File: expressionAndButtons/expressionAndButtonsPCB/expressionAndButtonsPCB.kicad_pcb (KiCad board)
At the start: 2 copper layers, 189.7 x 184.2 mm, 66 parts, among them J1 Alimentazione, J2 Input comandi, J3 OUTPUT C, J4 OUTPUT I, J5 OUTPUT III, J6 INPUT C-I-III, U2 ProMicro

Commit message: Progresso bottoniera
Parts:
- added J7: Conn_01x04, TerminalBlock_Phoenix:TerminalBlock_Phoenix_MPT-0,5-4-2.54_1x04_P2.54mm_Horizontal, F.Cu at (37.6, 105.4)
- added J8: Conn_01x04, TerminalBlock_Phoenix:TerminalBlock_Phoenix_MPT-0,5-4-2.54_1x04_P2.54mm_Horizontal, F.Cu at (214.4, 94.5)
- J2: value Input comandi -> Conn_01x12; footprint TerminalBlock_Phoenix:TerminalBlock_Phoenix_MKDS-1,5-16_1x16_P5.00mm_Horizontal -> TerminalBlock_Phoenix:TerminalBlock_Phoenix_MPT-0,5-12-2.54_1x12_P2.54mm_Horizontal
- J3: value OUTPUT C -> Conn_01x12; footprint TerminalBlock_Phoenix:TerminalBlock_Phoenix_MKDS-1,5-16_1x16_P5.00mm_Horizontal -> TerminalBlock_Phoenix:TerminalBlock_Phoenix_MPT-0,5-12-2.54_1x12_P2.54mm_Horizontal
- J4, J5: footprint TerminalBlock_Phoenix:TerminalBlock_Phoenix_MKDS-1,5-9-5.08_1x09_P5.08mm_Horizontal -> TerminalBlock_Phoenix:TerminalBlock_Phoenix_MPT-0,5-9-2.54_1x09_P2.54mm_Horizontal
- moved J3 19.9 mm to (214.4, 126.5)
- moved J2 14.7 mm to (37.6, 73.2)
- moved J4 8.93 mm to (90.4, 200.2)
- moved J5 8.52 mm to (147.3, 199.1)
- moved J6 6.73 mm to (38.4, 150.4)
- moved F1 5.22 mm to (56.6, 41.1)
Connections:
- Cresc2 pad 10: Net-(Cresc2-VCC) -> Net-(Cresc1-VCC)
- Cresc2 pad 13: Net-(Cresc2-VCC) -> Net-(Cresc1-VCC)
- Cresc2 pad 16: Net-(Cresc2-VCC) -> Net-(Cresc1-VCC)
- IN1 pad 7: Net-(IN1-~{Q7}) -> unconnected-(IN1-~{Q7}-Pad7)
- IN1 pad 9: unconnected-(IN1-Q7-Pad9) -> Net-(IN1-Q7)
- IN2 pad 10: Net-(IN1-~{Q7}) -> Net-(IN1-Q7)
- R29 pad 2: Net-(J3-Pin_13) -> Net-(J8-Pin_1)
- R30 pad 2: Net-(J3-Pin_14) -> Net-(J8-Pin_2)
- R31 pad 2: Net-(J3-Pin_15) -> Net-(J8-Pin_3)
- R32 pad 2: Net-(J3-Pin_16) -> Net-(J8-Pin_4)
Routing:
- net Net-(J6-Pin_3): track 0.00 -> 320.0 mm
- net Net-(J6-Pin_2): track 0.00 -> 312.7 mm
- net Net-(J6-Pin_1): track 0.00 -> 307.8 mm
- net Net-(Cresc1-VCC): track 101.4 -> 362.0 mm
- net Net-(IN2-D2): track 24.2 -> 179.5 mm
- net Net-(IN2-D3): track 24.1 -> 178.7 mm
- net Net-(IN2-D1): track 24.2 -> 176.2 mm
- net Net-(IN2-D7): track 24.1 -> 173.6 mm
- net Net-(IN2-D0): track 24.1 -> 172.7 mm
- net Net-(Cresc1-QA): track 0.00 -> 147.2 mm
- net Net-(IN2-D6): track 24.2 -> 164.2 mm
- net Net-(Cresc1-QB): track 0.00 -> 132.0 mm
- net Net-(IN2-D5): track 24.2 -> 155.6 mm
- net Net-(Cresc1-QC): track 0.00 -> 124.9 mm
- net Net-(IN2-D4): track 24.1 -> 145.6 mm
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
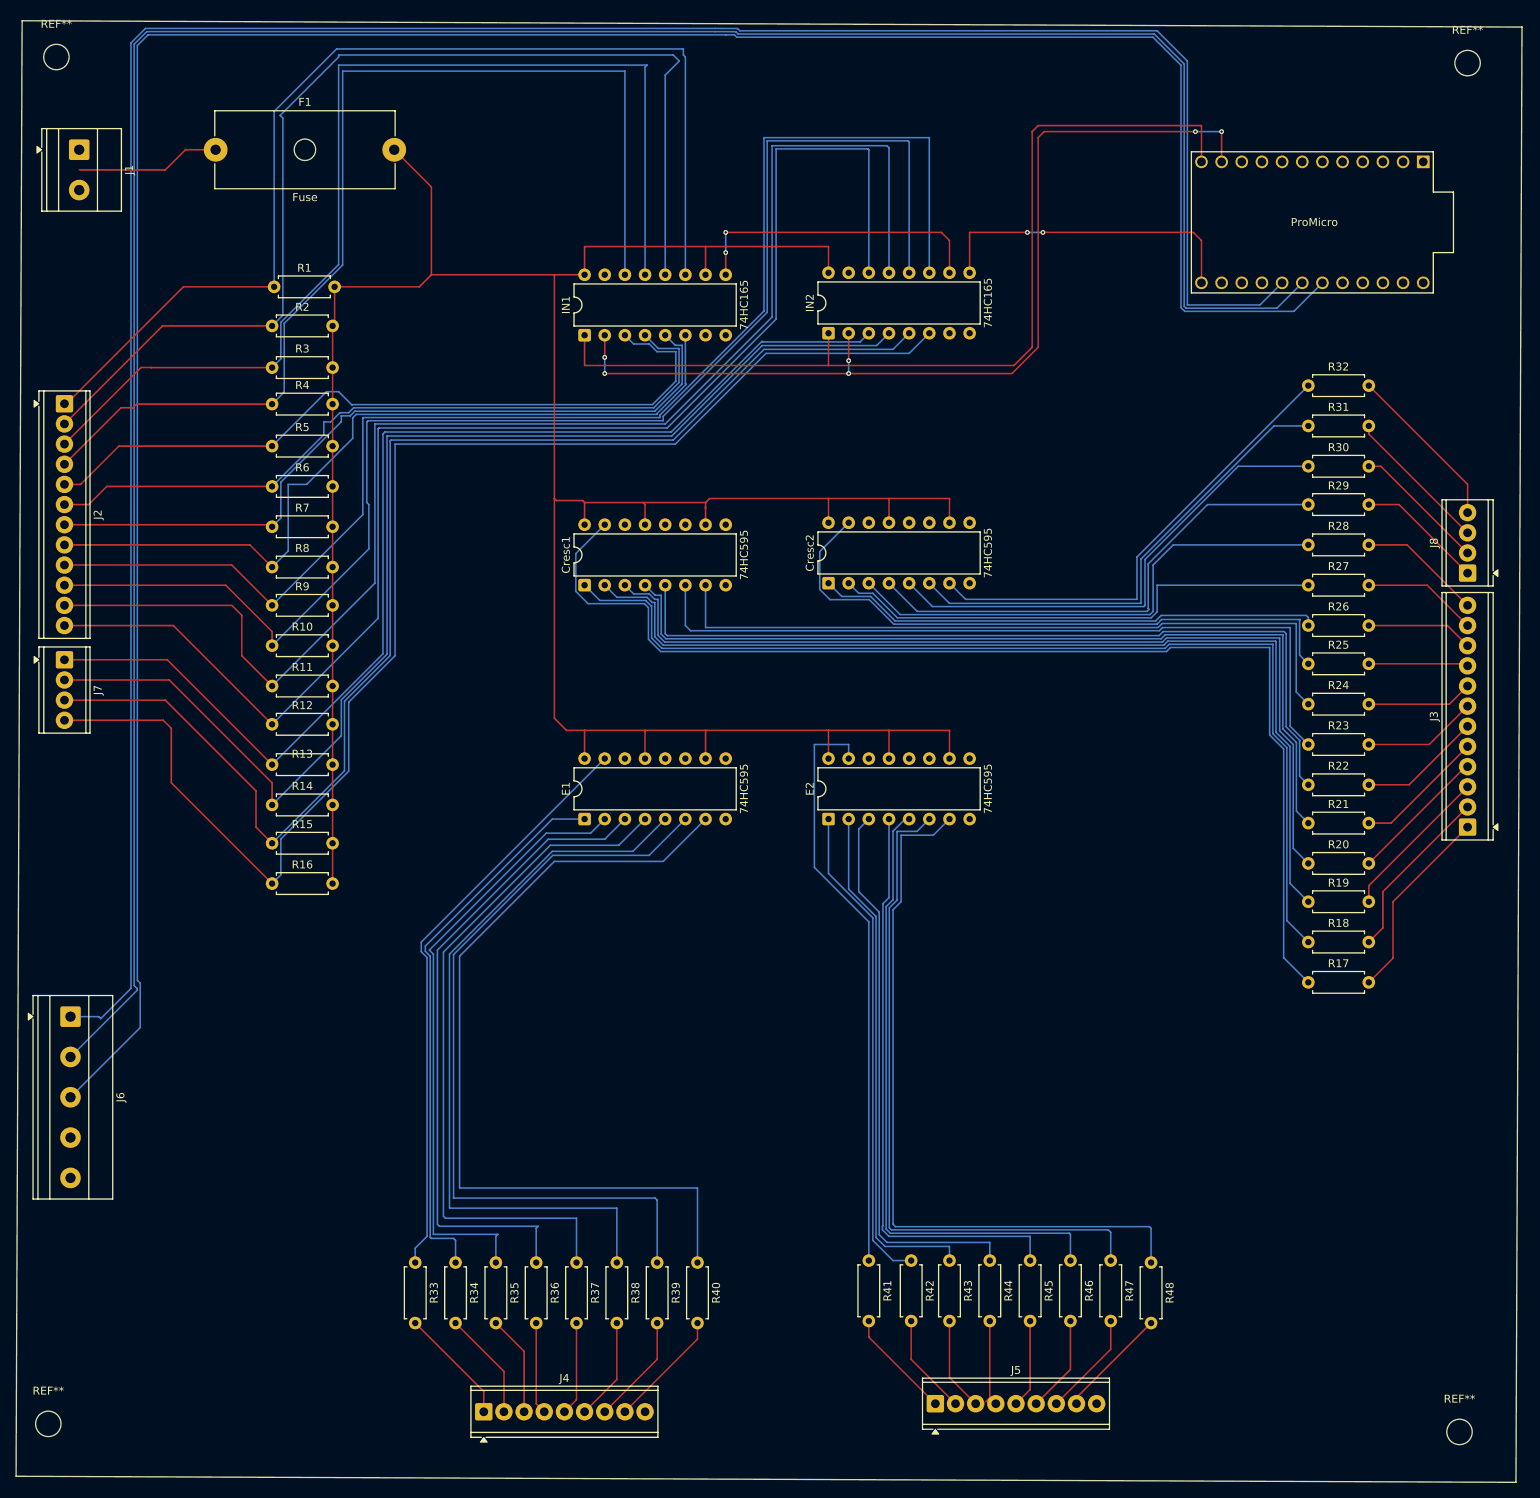
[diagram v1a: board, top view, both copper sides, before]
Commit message: First version buttons
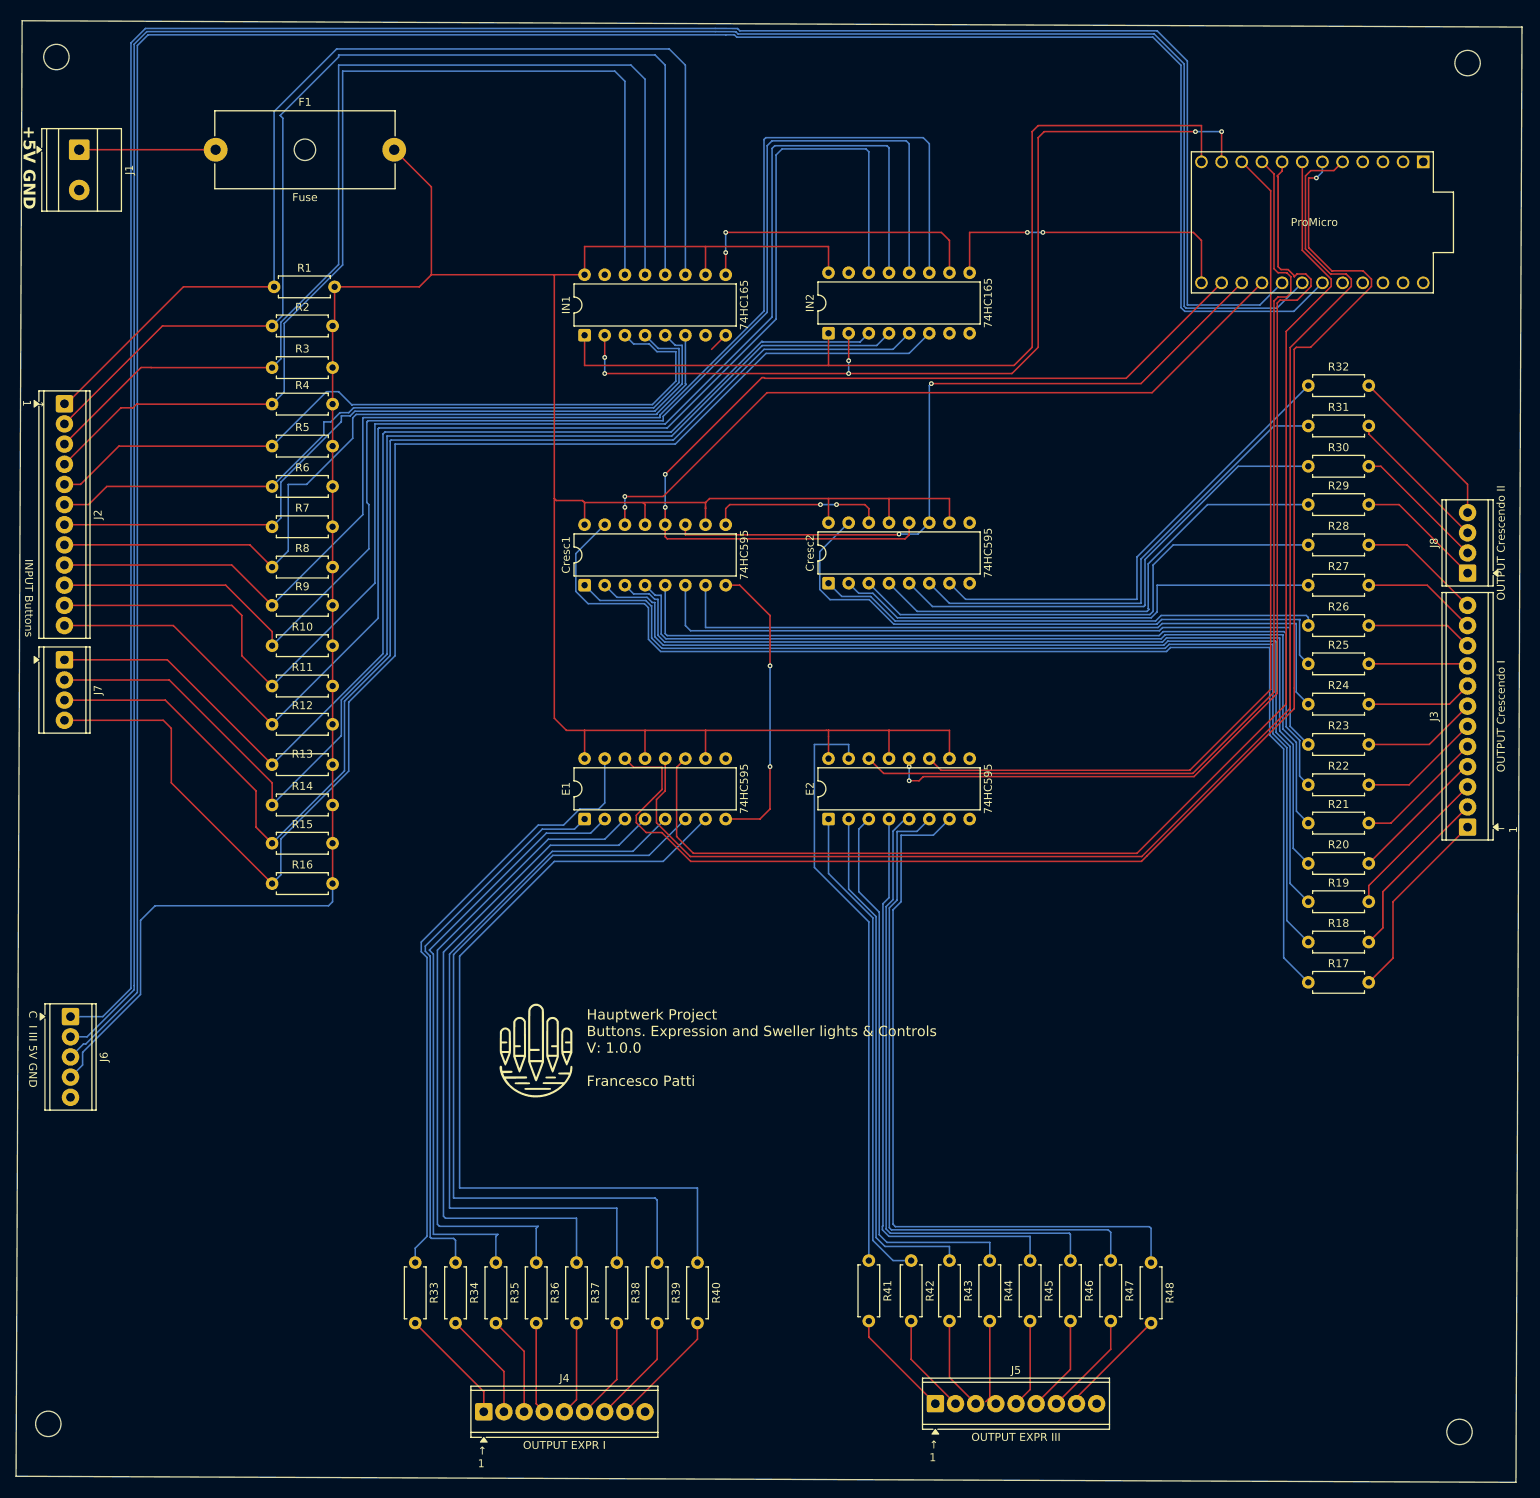
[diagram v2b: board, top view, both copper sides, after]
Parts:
- added G***: LOGO, logo_lib:logo_serigrafia, F.Cu at (97.0, 154.7)
- J3: value Conn_01x12 -> OUTPUT Crescendo I
- J4: value OUTPUT I -> OUTPUT EXPR I
- J5: value OUTPUT III -> OUTPUT EXPR III
- J6: footprint TerminalBlock_Phoenix:TerminalBlock_Phoenix_MKDS-1,5-5-5.08_1x05_P5.08mm_Horizontal -> TerminalBlock_Phoenix:TerminalBlock_Phoenix_MPT-0,5-5-2.54_1x05_P2.54mm_Horizontal
- J8: value Conn_01x04 -> OUTPUT Crescendo II
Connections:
- J1 pad 1: GND -> +5V
- J1 pad 2: +5V -> GND
- J6 pad 4: +5V -> Net-(Cresc1-VCC)
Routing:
- net Net-(E1-SER): track 0.00 -> 187.2 mm, vias 0 -> 1
- net Net-(E1-RCLK): track 0.00 -> 177.1 mm
- net Net-(E1-SRCLK): track 0.00 -> 167.9 mm
- net Net-(E2-RCLK): track 0.00 -> 127.6 mm, vias 0 -> 2
- net Net-(E2-SER): track 0.00 -> 126.6 mm
- net Net-(Cresc1-RCLK): track 0.00 -> 120.6 mm, vias 0 -> 2
- net Net-(E2-SRCLK): track 0.00 -> 115.8 mm
- net Net-(Cresc1-SER): track 0.00 -> 95.0 mm, vias 0 -> 2
- net Net-(Cresc1-SRCLK): track 0.00 -> 94.6 mm, vias 0 -> 2
- net Net-(Cresc1-VCC): track 362.0 -> 412.8 mm
- net GND: track 0.00 -> 40.2 mm, vias 0 -> 2
- net Net-(Cresc1-QH'): track 0.00 -> 22.3 mm, vias 0 -> 2
- net Net-(J6-Pin_3): track 320.0 -> 314.8 mm
- net Net-(E1-QA): track 74.0 -> 77.3 mm
- net Net-(IN1-D1): track 140.4 -> 137.6 mm
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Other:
- board text added: "+5V GND"
- board text added: "C I III 5V GND"
- board text added: "Hauptwerk Project Buttons. Expression and Sweller lights & Controls V: 1.0.0 Francesco Patti"
- board text added: "INPUT Buttons"
- board text added: "↑ 1"

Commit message: update
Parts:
- J1: footprint TerminalBlock_Phoenix:TerminalBlock_Phoenix_MKDS-1,5-2-5.08_1x02_P5.08mm_Horizontal -> TerminalBlock_Phoenix:TerminalBlock_Phoenix_MPT-0,5-2-2.54_1x02_P2.54mm_Horizontal
- J4: value OUTPUT EXPR I -> OUTPUT I
- J5: value OUTPUT EXPR III -> OUTPUT III
- moved REF** 30.7 mm to (213.6, 172.0)
- moved J5 30.3 mm to (149.0, 168.9)
- moved R41 30.3 mm to (140.6, 150.9)
- moved R42 30.3 mm to (145.9, 150.9)
- moved R43 30.3 mm to (150.7, 150.9)
- moved R44 30.3 mm to (155.8, 150.9)
- moved R45 30.3 mm to (160.9, 150.9)
- moved R46 30.3 mm to (166.0, 150.9)
- moved R47 30.3 mm to (171.1, 150.9)
- moved R48 30.3 mm to (176.1, 151.1)
- moved R33 30.2 mm to (84.0, 151.3)
- moved R34 30.2 mm to (89.1, 151.3)
- moved R35 30.2 mm to (94.1, 151.3)
- moved R36 30.2 mm to (99.2, 151.3)
- moved R37 30.2 mm to (104.3, 151.3)
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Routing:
- net GND: track 40.2 -> 177.5 mm
- net Net-(IN2-Q7): track 40.0 -> 83.1 mm
- net Net-(E1-QC): track 76.8 -> 42.5 mm
- net Net-(E1-QD): track 82.5 -> 49.0 mm
- net Net-(E1-QE): track 88.1 -> 55.4 mm
- net Net-(E1-QF): track 94.2 -> 62.0 mm
- net Net-(E1-QG): track 100.6 -> 68.5 mm
- net Net-(E1-QB): track 69.8 -> 37.8 mm
- net Net-(E1-QH): track 106.7 -> 74.9 mm
- net Net-(E2-QH): track 93.4 -> 62.0 mm
- net Net-(E2-QG): track 87.6 -> 56.5 mm
- net Net-(E2-QF): track 80.0 -> 49.2 mm
- net Net-(E2-QE): track 74.1 -> 43.6 mm
- net Net-(E2-QD): track 70.6 -> 40.5 mm
- net Net-(E2-QC): track 65.6 -> 35.9 mm
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- added copper zone on F.Cu, net GND
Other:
- board size 189.7 x 184.2 mm -> 189.2 x 156.1 mm
- board text added: "1->"

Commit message: problem fix
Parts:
- removed J8: OUTPUT Crescendo II, TerminalBlock_Phoenix:TerminalBlock_Phoenix_MPT-0,5-4-2.54_1x04_P2.54mm_Horizontal
- added J9: Conn_01x10, TerminalBlock_Phoenix:TerminalBlock_Phoenix_MPT-0,5-10-2.54_1x10_P2.54mm_Horizontal, F.Cu at (39.9, 67.1)
- J2: value Conn_01x12 -> Conn_01x06; footprint TerminalBlock_Phoenix:TerminalBlock_Phoenix_MPT-0,5-12-2.54_1x12_P2.54mm_Horizontal -> TerminalBlock_Phoenix:TerminalBlock_Phoenix_MPT-0,5-6-2.54_1x06_P2.54mm_Horizontal
- J3: value OUTPUT Crescendo I -> Conn_01x10; footprint TerminalBlock_Phoenix:TerminalBlock_Phoenix_MPT-0,5-12-2.54_1x12_P2.54mm_Horizontal -> TerminalBlock_Phoenix:TerminalBlock_Phoenix_MPT-0,5-10-2.54_1x10_P2.54mm_Horizontal
- J7: value Conn_01x04 -> Conn_01x06; footprint TerminalBlock_Phoenix:TerminalBlock_Phoenix_MPT-0,5-4-2.54_1x04_P2.54mm_Horizontal -> TerminalBlock_Phoenix:TerminalBlock_Phoenix_MPT-0,5-6-2.54_1x06_P2.54mm_Horizontal
- moved J7 176.7 mm to (214.2, 99.5), turned to 90 degrees
- moved J2 21.6 mm to (39.9, 94.6)
- moved J3 0.20 mm to (214.2, 126.5)
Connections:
- Cresc1 pad 13: Net-(Cresc1-VCC) -> GND
- Cresc2 pad 13: Net-(Cresc1-VCC) -> GND
- E1 pad 13: Net-(Cresc1-VCC) -> GND
- E2 pad 13: Net-(Cresc1-VCC) -> GND
- J2 pad 1: Net-(IN1-D0) -> Net-(IN2-D2)
- J2 pad 2: Net-(IN1-D1) -> Net-(IN2-D3)
- J2 pad 3: Net-(IN1-D2) -> Net-(IN2-D4)
- J2 pad 4: Net-(IN1-D3) -> Net-(IN2-D5)
- J2 pad 5: Net-(IN1-D4) -> Net-(IN2-D6)
- J2 pad 6: Net-(IN1-D5) -> Net-(IN2-D7)
- J7 pad 1: Net-(IN2-D4) -> Net-(J7-Pin_1)
- J7 pad 2: Net-(IN2-D5) -> Net-(J7-Pin_2)
- J7 pad 3: Net-(IN2-D6) -> Net-(J7-Pin_3)
- J7 pad 4: Net-(IN2-D7) -> Net-(J7-Pin_4)
- R27 pad 2: Net-(J3-Pin_11) -> Net-(J7-Pin_1)
- R28 pad 2: Net-(J3-Pin_12) -> Net-(J7-Pin_2)
- R29 pad 2: Net-(J8-Pin_1) -> Net-(J7-Pin_3)
- R30 pad 2: Net-(J8-Pin_2) -> Net-(J7-Pin_4)
- R31 pad 2: Net-(J8-Pin_3) -> Net-(J7-Pin_5)
- R32 pad 2: Net-(J8-Pin_4) -> Net-(J7-Pin_6)
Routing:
- net GND: track 177.5 -> 228.0 mm
- net Net-(J8-Pin_4): track 21.2 -> 0.00 mm
- net Net-(J7-Pin_6): track 0.00 -> 21.0 mm
- net Net-(J8-Pin_3): track 18.6 -> 0.00 mm
- net Net-(J7-Pin_5): track 0.00 -> 18.5 mm
- net Net-(J8-Pin_2): track 17.0 -> 0.00 mm
- net Net-(J7-Pin_4): track 0.00 -> 16.8 mm
- net Net-(J8-Pin_1): track 16.0 -> 0.00 mm
- net Net-(J7-Pin_3): track 0.00 -> 15.8 mm
- net Net-(J3-Pin_12): track 15.6 -> 0.00 mm
- net Net-(J7-Pin_2): track 0.00 -> 14.8 mm
- net Net-(J3-Pin_11): track 14.6 -> 0.00 mm
- net Net-(J7-Pin_1): track 0.00 -> 13.7 mm
- net Net-(Cresc1-VCC): track 412.6 -> 399.5 mm
- net Net-(IN1-D2): track 135.8 -> 130.9 mm
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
